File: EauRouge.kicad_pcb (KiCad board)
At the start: 4 copper layers, 50 x 50 mm, 66 parts, among them J1 XT30PW-M, J2 SM05B-GHS-TB, J3 1985807, J4 PH1RA-03-UA, J5 PH1RA-03-UA, Q1 DMN3731U-7, Q2 DMN3731U-7, U1 113991054, U2 SN74LVC2G17DBVR, U3 LMR51420YDDCR, U4 LM317MDCYR

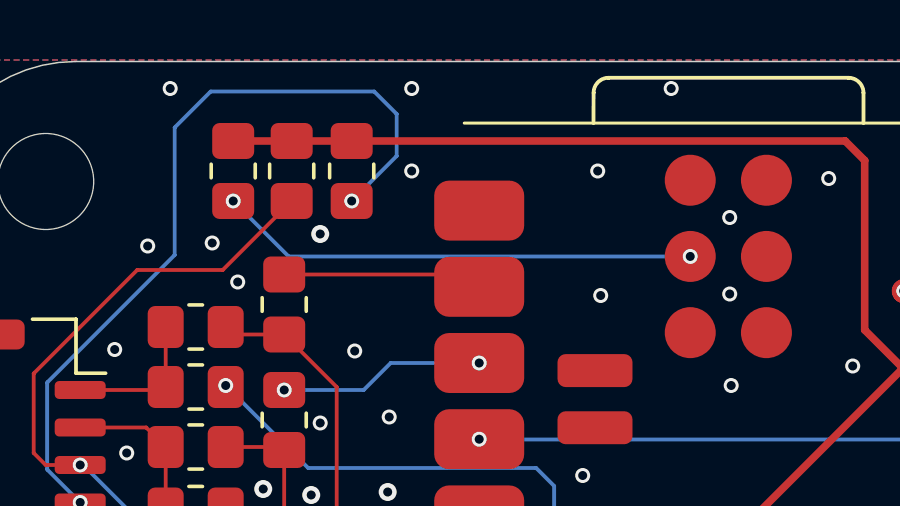
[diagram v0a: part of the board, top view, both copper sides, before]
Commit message: removed duplicated pullup resistor on chip en
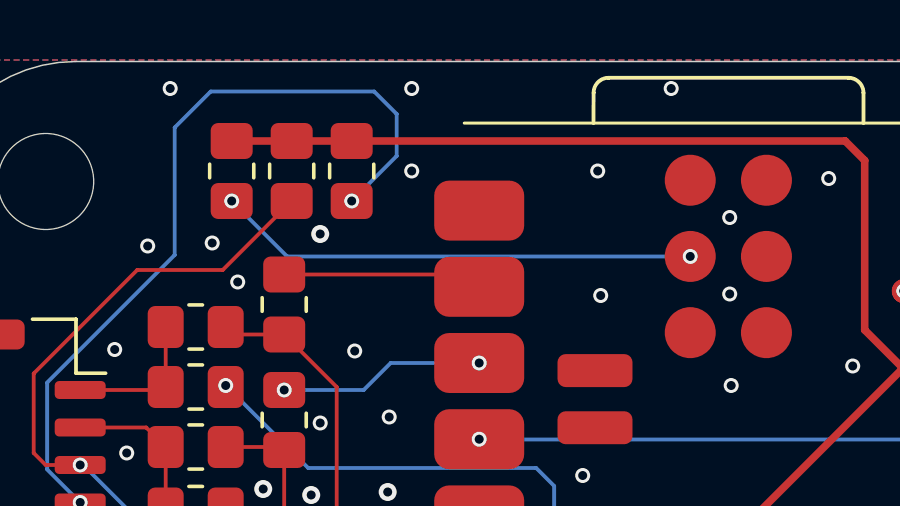
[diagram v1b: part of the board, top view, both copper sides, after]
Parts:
- R3: value RMCF0805JT4K70 -> DNP 0805
- turned R3 to 90 degrees
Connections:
- R3 pad 1: +3.3V -> /MCU/CHIP_EN
- R3 pad 2: /MCU/CHIP_EN -> +3.3V
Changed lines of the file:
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@@
 	(footprint "Resistor_SMD:R_0805_2012Metric_Pad1.20x1.40mm_HandSolder"
 		(layer "F.Cu")
-		(at 110.25 103.65 -90)
+		(at 110.2 103.65 90)
 		(descr "Resistor SMD 0805 (2012 Metric), square (rectangular) end terminal, IPC_7351 nominal with elongated pad for handsoldering. (Body size source: IPC-SM-782 page 72, https://www.pcb-3d.com/wordpress/wp-content/uploads/ipc-sm-782a_amendment_1_and_2.pdf), generated with kicad-footprint-generator")
 		(tags "resistor handsolder")
@@
 			)
 		)
-		(property "Value" "RMCF0805JT4K70"
+		(property "Value" "DNP 0805"
 			(at 0 1.65 90)
 			(layer "F.Fab")
@@
 		)
 		(property "Footprint" "Resistor_SMD:R_0805_2012Metric_Pad1.20x1.40mm_HandSolder"
-			(at 0 0 -90)
+			(at 0 0 90)
 			(unlocked yes)
 			(layer "F.Fab")
@@
 		)
 		(property "Datasheet" ""
-			(at 0 0 -90)
+			(at 0 0 90)
 			(unlocked yes)
 			(layer "F.Fab")
@@
 			)
 		)
-		(property "Description" "RES 4.7K OHM 5% 1/8W 0805"
-			(at 0 0 -90)
+		(property "Description" "Res 0805 Do Not Populate"
+			(at 0 0 90)
 			(unlocked yes)
 			(layer "F.Fab")
@@
 		)
 		(property "PARTREV" "V.12"
-			(at 0 0 -90)
+			(at 0 0 90)
 			(unlocked yes)
 			(layer "F.Fab")
@@
 		)
 		(property "STANDARD" "IPC 7351B"
-			(at 0 0 -90)
+			(at 0 0 90)
 			(unlocked yes)
 			(layer "F.Fab")
@@
 		)
 		(property "MAXIMUM_PACKAGE_HEIGHT" "0.6 mm"
-			(at 0 0 -90)
+			(at 0 0 90)
 			(unlocked yes)
 			(layer "F.Fab")
@@
 		)
 		(property "MANUFACTURER" "Yageo"
-			(at 0 0 -90)
+			(at 0 0 90)
 			(unlocked yes)
 			(layer "F.Fab")
@@
 			)
 		)
-		(property "Resistance" "4.7kΩ"
-			(at 0 0 -90)
+		(property "Resistance" "DNP"
+			(at 0 0 90)
 			(unlocked yes)
 			(layer "F.Fab")
@@
 			)
 		)
-		(property "Tolerance" "5%"
-			(at 0 0 -90)
+		(property "Tolerance" "-"
+			(at 0 0 90)
 			(unlocked yes)
 			(layer "F.Fab")
@@
 		)
 		(property "Power" "1/8W"
-			(at 0 0 -90)
+			(at 0 0 90)
 			(unlocked yes)
 			(layer "F.Fab")
@@
 		)
 		(property "Package" "0805"
-			(at 0 0 -90)
+			(at 0 0 90)
 			(unlocked yes)
 			(layer "F.Fab")
@@
 		(attr smd)
 		(fp_line
-			(start -0.227064 0.735)
-			(end 0.227064 0.735)
+			(start -0.227064 -0.735)
+			(end 0.227064 -0.735)
 			(stroke
 				(width 0.12)
@@
 		)
 		(fp_line
-			(start -0.227064 -0.735)
-			(end 0.227064 -0.735)
+			(start -0.227064 0.735)
+			(end 0.227064 0.735)
 			(stroke
 				(width 0.12)
@@
 		)
 		(fp_line
-			(start -1.85 0.95)
-			(end -1.85 -0.95)
+			(start 1.85 -0.95)
+			(end 1.85 0.95)
 			(stroke
 				(width 0.05)
@@
 		)
 		(fp_line
-			(start 1.85 0.95)
-			(end -1.85 0.95)
+			(start -1.85 -0.95)
+			(end 1.85 -0.95)
 			(stroke
 				(width 0.05)
@@
 		)
 		(fp_line
-			(start -1.85 -0.95)
-			(end 1.85 -0.95)
+			(start 1.85 0.95)
+			(end -1.85 0.95)
 			(stroke
 				(width 0.05)
@@
 		)
 		(fp_line
-			(start 1.85 -0.95)
-			(end 1.85 0.95)
+			(start -1.85 0.95)
+			(end -1.85 -0.95)
 			(stroke
 				(width 0.05)
@@
 		)
 		(fp_line
-			(start -1 0.625)
-			(end -1 -0.625)
+			(start 1 -0.625)
+			(end 1 0.625)
 			(stroke
 				(width 0.1)
@@
 		)
 		(fp_line
-			(start 1 0.625)
-			(end -1 0.625)
+			(start -1 -0.625)
+			(end 1 -0.625)
 			(stroke
 				(width 0.1)
@@
 		)
 		(fp_line
-			(start -1 -0.625)
-			(end 1 -0.625)
+			(start 1 0.625)
+			(end -1 0.625)
 			(stroke
 				(width 0.1)
@@
 		)
 		(fp_line
-			(start 1 -0.625)
-			(end 1 0.625)
+			(start -1 0.625)
+			(end -1 -0.625)
 			(stroke
 				(width 0.1)
@@
 		)
 		(pad "1" smd roundrect
-			(at -1 0 270)
+			(at -1 0 90)
 			(size 1.2 1.4)
 			(layers "F.Cu" "F.Paste" "F.Mask")
 			(roundrect_rratio 0.208333)
-			(net 4 "+3.3V")
+			(net 18 "/MCU/CHIP_EN")
 			(pintype "passive")
 			(solder_mask_margin 0.05)
 		)
 		(pad "2" smd roundrect
-			(at 1 0 270)
+			(at 1 0 90)
 			(size 1.2 1.4)
 			(layers "F.Cu" "F.Paste" "F.Mask")
 			(roundrect_rratio 0.208333)
-			(net 18 "/MCU/CHIP_EN")
+			(net 4 "+3.3V")
 			(pintype "passive")
 			(solder_mask_margin 0.05)
@@
 		(property ki_fp_filters "MountingHole*")
 		(sheetname "Root")
-		(sheetfile "Spa-Eau_Rouge.kicad_sch")
+		(sheetfile "EauRouge.kicad_sch")
 		(attr exclude_from_pos_files exclude_from_bom)
 		(fp_circle
@@
 		)
 		(sheetname "Root")
-		(sheetfile "Spa-Eau_Rouge.kicad_sch")
+		(sheetfile "EauRouge.kicad_sch")
 		(attr through_hole)
 		(fp_line
@@
 		)
 		(sheetname "Root")
-		(sheetfile "Spa-Eau_Rouge.kicad_sch")
+		(sheetfile "EauRouge.kicad_sch")
 		(attr through_hole)
 		(fp_line
@@
 		(property ki_fp_filters "MountingHole*")
 		(sheetname "Root")
-		(sheetfile "Spa-Eau_Rouge.kicad_sch")
+		(sheetfile "EauRouge.kicad_sch")
 		(attr exclude_from_pos_files exclude_from_bom)
 		(fp_circle
@@
 		)
 		(sheetname "Root")
-		(sheetfile "Spa-Eau_Rouge.kicad_sch")
+		(sheetfile "EauRouge.kicad_sch")
 		(attr smd)
 		(fp_line
@@
 		(property ki_fp_filters "TerminalBlock*:*")
 		(sheetname "Root")
-		(sheetfile "Spa-Eau_Rouge.kicad_sch")
+		(sheetfile "EauRouge.kicad_sch")
 		(attr through_hole)
 		(fp_line
@@
 		(property ki_fp_filters "MountingHole*")
 		(sheetname "Root")
-		(sheetfile "Spa-Eau_Rouge.kicad_sch")
+		(sheetfile "EauRouge.kicad_sch")
 		(attr exclude_from_pos_files exclude_from_bom)
 		(fp_circle
@@
 		(property ki_fp_filters "MountingHole*")
 		(sheetname "Root")
-		(sheetfile "Spa-Eau_Rouge.kicad_sch")
+		(sheetfile "EauRouge.kicad_sch")
 		(attr exclude_from_pos_files exclude_from_bom)
 		(fp_circle
@@
 		)
 		(sheetname "Root")
-		(sheetfile "Spa-Eau_Rouge.kicad_sch")
+		(sheetfile "EauRouge.kicad_sch")
 		(attr through_hole)
 		(fp_line
@@
 	)
 	(via
-		(at 110.25 104.65)
+		(at 110.2 104.65)
 		(size 0.5)
 		(drill 0.3)
@@
 	)
 	(segment
-		(start 125.483 106.5)
-		(end 112.1 106.5)
+		(start 110.2 104.65)
+		(end 112.05 106.5)
 		(width 0.127)
 		(layer "B.Cu")
@@
 	)
 	(segment
-		(start 125.485 106.498)
-		(end 125.483 106.5)
+		(start 125.483 106.5)
+		(end 125.485 106.498)
 		(width 0.127)
 		(layer "B.Cu")
@@
 	)
 	(segment
-		(start 112.1 106.5)
-		(end 110.25 104.65)
+		(start 112.05 106.5)
+		(end 125.483 106.5)
 		(width 0.127)
 		(layer "B.Cu")
